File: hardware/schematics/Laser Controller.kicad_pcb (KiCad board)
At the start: 2 copper layers, 175 x 115 mm, 99 parts, among them J1 SD Card Module (6-pin, 2.54mm), J2 PWR IN +5V, J3 PWR IN Galvo, J4 FAN1 PWR IN, J5 FAN1, J6 FAN2 PWR IN, J7 FAN2, U1 ESP32-S3-N16R8-DevKit, U10 DS18B20, U12 OPA4134UA_2K5, U13 Galvo Input, U15 6N137, U16 6N137, U17 6N137, U2 DAC8562SDGST, U3 TTL_RGB Blue, U4 TTL_RGB Red, U5 TTL_RGB Green, U6 DS18B20, U7 DS18B20, U8 DS18B20, U9 DS18B20

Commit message: hw: v6.86.0 -- J3 and J_DMX finally get real JST-XH bodies, DS18B20 quintet marches into a single file
- J3 (PWR IN Galvo) and J_DMX: swapped the leftover PinSocket-shaped copper
  for the actual JST_XH_B4B-XH-A_1x04 pads/courtyard/silk (previous pass only
  renamed the footprint field, geometry never followed). Repositioned/rotated
  to match, all nets re-verified pad-for-pad against the old routing.
- U6-U10 (DS18B20): the two-column layout put real B3B-XH-A housings only
  9mm apart (need ~11mm not to collide) -- courtyards overlapped by ~2x6.8mm.
  Collapsed all five into one vertical column with >=9mm pitch (one wider
  gap to dodge R31), rebuilt the DS18B20_1WIRE and +3V3 local bus wiring
  (two vias added to hop the existing +3V3 trunk crossing) to match.
- Verified: check_courtyard_overlaps clean for all six connectors, no new
  shorts/crossings introduced (DRC-diffed against baseline).

Known follow-up (not touched this round, needs a call):
- U13 (Galvo Input) footprint field says JST_XH_B3B-XH-A_1x03 but the
  placed copper is 4 SMD pads that don't match a 3-pin THT JST at all --
  worse than the J3/J_DMX bug, needs the real part identified first.
- J2 (PWR IN +5V) has the exact same label-only bug J3 had: JST_XH_B2B-XH-A
  in the footprint field, old PinSocket-shaped copper underneath.
- Zone refill needed in KiCad (Edit > Fill Zones, hotkey B) -- the GND pour
  wasn't recomputed around the new copper, so DRC still shows stale
  zone-clearance/solder-mask-bridge noise at the new pad/via spots until
  that runs. MCP's own refill_zones has a known segfault risk on this
  backend, so left it for the UI.
- Pre-existing +3V3/FAN1_PWM clearance nits near U3 and the top-left
  starved-thermal/silk warnings untouched, as requested.
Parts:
- removed the J_DMX at (236.0, 60.0)
- added J_DMX: DMX MAX485, Connector_JST:JST_XH_B4B-XH-A_1x04_P2.50mm_Vertical, F.Cu at (236.0, 60.0)
- moved U10 33.2 mm to (184.6, 140.1)
- moved U9 28.5 mm to (184.6, 127.1)
- moved U8 2.00 mm to (184.6, 118.1)
- moved U7 1.00 mm to (184.6, 109.1)
- turned J3 to -90 degrees
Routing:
- net DS18B20_1WIRE: track 157.2 -> 144.6 mm, vias 1 -> 4
- net +3V3: track 374.5 -> 378.1 mm

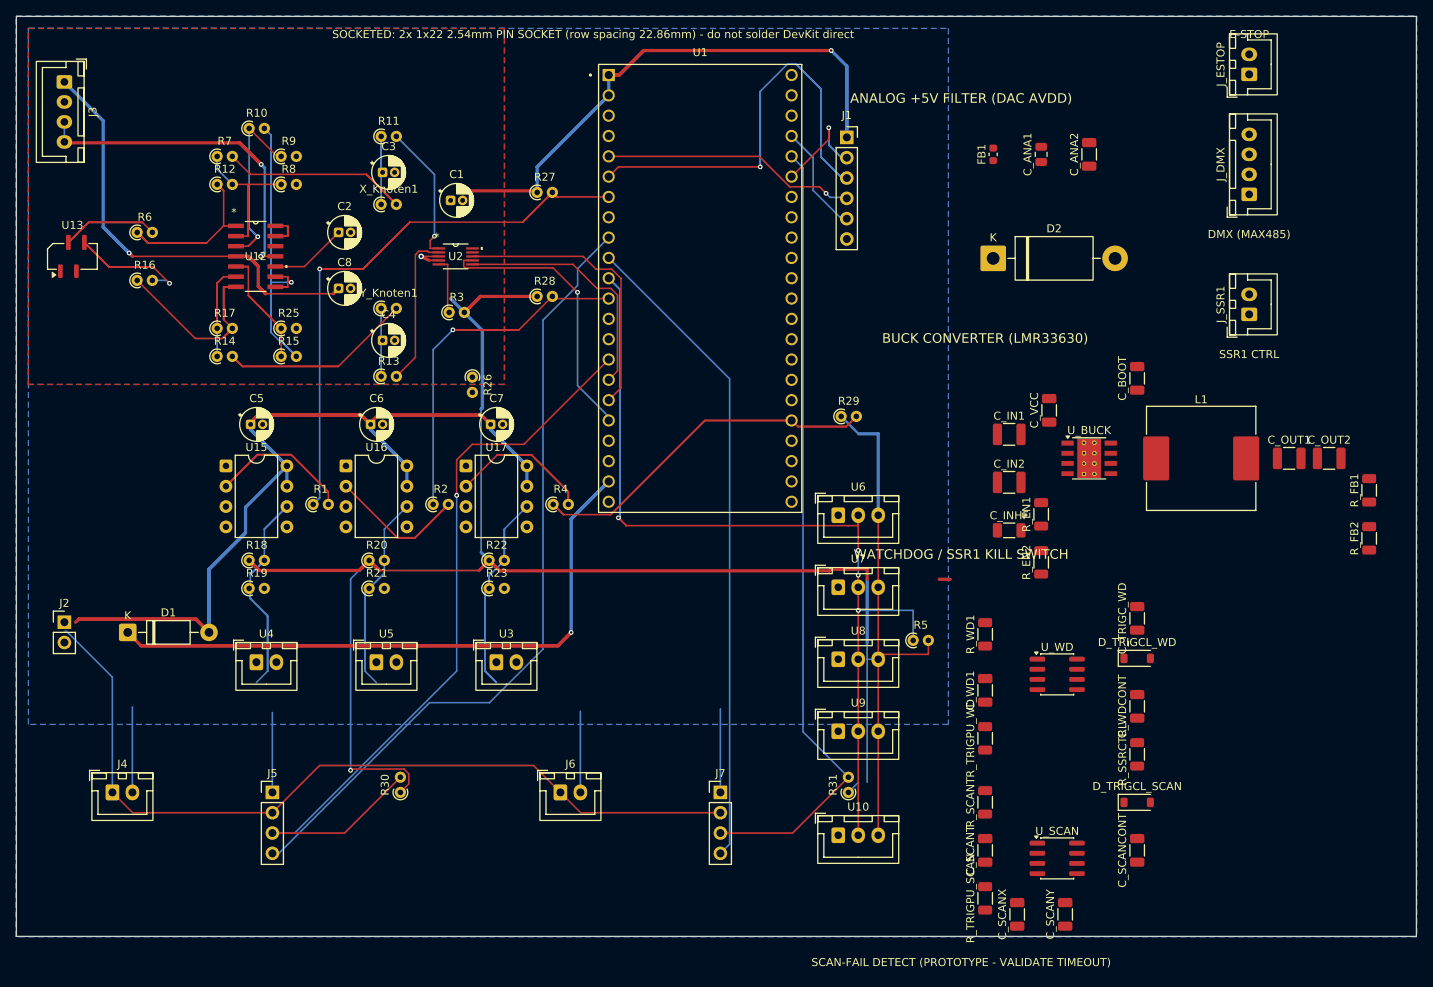
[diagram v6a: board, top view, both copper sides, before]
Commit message: hw: v6.88.0 -- the axial resistors trade their leads for landing pads
Swapped 32 THT axial resistors (all the 1k/10k/22k pull-ups, dividers,
and 0-ohm jumpers) plus 8 miswired-footprint decoupling caps from
CP_Radial to real Capacitor_SMD, all onto 1206 SMD to match the rest
of the board's existing SMD convention. Buck output caps C_OUT1/2
downsized 1210->1206 (5V rail, plenty of voltage margin).

Left alone on purpose: C_IN1/C_IN2 stay 1210 (10-30V input needs a
voltage rating 1206 can't reliably deliver at 10uF), L1 stays a real
shielded power inductor (no chip inductor eats buck-converter amps),
FB1 stays 0603 (already smaller than asked for).

Routing is now stale -- pad positions moved, so this needs a
re-place + re-route pass in KiCad before it's fab-ready.
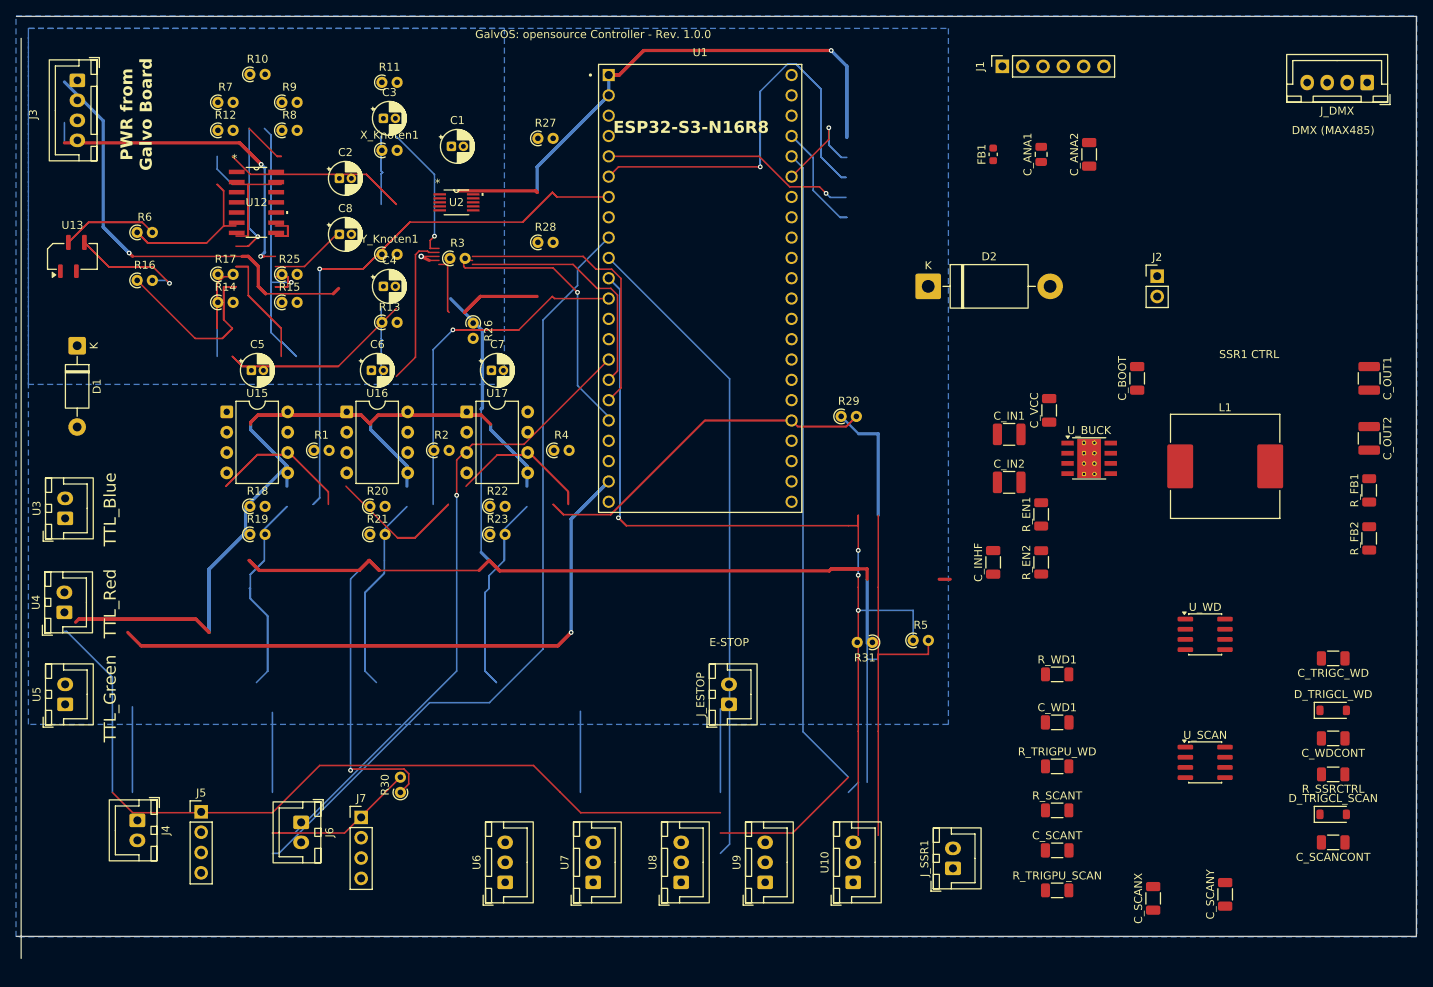
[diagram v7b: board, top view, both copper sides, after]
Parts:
- C1, C2, C3, C4, C5, C6, C7, C8: footprint CP_Radial_D4.0mm_P1.50mm -> Capacitor_SMD:C_1206_3216Metric
- C_OUT1, C_OUT2: footprint Capacitor_SMD:C_1210_3225Metric -> Capacitor_SMD:C_1206_3216Metric
- R1, R10, R11, R12, R13, R14, R15, R16, R17, R18, R19, R2, R20, R21, R22, R23, R25, R26, R27, R28, R29, R3, R4, R5, R6, R7, R8, R9, X_Knoten1, Y_Knoten1: footprint R_Axial_DIN0204_L3.6mm_D1.6mm_P1.90mm_Vertical -> Resistor_SMD:R_1206_3216Metric
- R30, R31: footprint Resistor_THT:R_Axial_DIN0204_L3.6mm_D1.6mm_P1.90mm_Vertical -> Resistor_SMD:R_1206_3216Metric
- U13: value Galvo Input -> Galvo Output
- moved J2 143.3 mm to (224.5, 70.2)
- moved J_ESTOP 102.1 mm to (171.0, 123.8)
- moved J_SSR1 78.5 mm to (199.0, 144.2)
- moved U6 62.0 mm to (143.0, 146.0), turned to 90 degrees
- moved U3 56.8 mm to (88.0, 100.5), turned to 90 degrees
- moved U7 47.9 mm to (154.0, 146.0), turned to 90 degrees
- moved J7 45.0 mm to (125.0, 137.9)
- moved U5 39.3 mm to (88.0, 123.8), turned to 90 degrees
- moved D1 36.4 mm to (89.5, 78.9), turned to -90 degrees
- moved U8 34.1 mm to (165.0, 146.0), turned to 90 degrees
- moved J6 32.6 mm to (117.5, 138.5), turned to -90 degrees
- moved D_TRIGCL_WD 25.3 mm to (246.5, 124.5)
- moved C_TRIGC_WD 25.0 mm to (246.5, 118.0), turned to 180 degrees
- moved C_WDCONT 24.8 mm to (246.5, 128.0), turned to 180 degrees
- moved U4 24.8 mm to (87.9, 112.2), turned to 90 degrees
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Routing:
- net 5V GND Buck: track 41.3 -> 275.1 mm
- net Buck +5V: track 288.7 -> 117.4 mm
- net VREF_BUF: track 67.1 -> 0.00 mm, vias 1 -> 0
- net Net-(U12-+IN_B): track 21.8 -> 89.0 mm, vias 0 -> 1
- net +3V3: track 378.1 -> 325.4 mm
- net AGND (from Galvo Board): track 4.55 -> 49.3 mm
- net Net-(U15-A): track 34.3 -> 0.00 mm
- net Net-(U17-A): track 30.3 -> 0.00 mm
- net DS18B20_1WIRE: track 144.6 -> 171.4 mm
- net TTL_RGB_GREEN: track 38.0 -> 60.8 mm
- net FAN2_TACH: track 99.4 -> 80.6 mm
- net TTL_RGB_BLUE: track 42.1 -> 30.3 mm
- net Net-(U12-+IN_C): track 9.67 -> 0.00 mm
- net +15V: track 63.2 -> 72.9 mm
- net TTL_RGB_RED: track 43.2 -> 34.3 mm
- removed copper zone on F.Cu, net AGND (from Galvo Board)
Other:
- board size 175 x 115 mm -> 175 x 117.7 mm
- board text added: "ESP32-S3-N16R8"
- board text added: "GalvOS: opensource Controller - Rev. 1.0.0"
- board text added: "PWR from Galvo Board"
- board text added: "TTL_Blue"
- board text added: "TTL_Green"
- board text added: "TTL_Red"
- board text removed: "ANALOG +5V FILTER (DAC AVDD)"
- board text removed: "BUCK CONVERTER (LMR33630)"
- board text removed: "SCAN-FAIL DETECT (PROTOTYPE - VALIDATE TIMEOUT)"
- board text removed: "SOCKETED: 2x 1x22 2.54mm PIN SOCKET (row spacing 22.86mm) - do not solder DevKit direct"
- board text removed: "WATCHDOG / SSR1 KILL SWITCH"
